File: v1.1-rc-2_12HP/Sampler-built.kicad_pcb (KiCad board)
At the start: 4 copper layers, 60.5 x 109.2 mm, 231 parts, among them J10 Eurorack_Power_10pin_Unshroud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, J11 3.5mm_Mono_Switched, J12 3.5mm_Mono_Switched, J13 3.5mm_Mono_Switched, J14 3.5mm_Mono_Switched, J15 3.5mm_Mono_Switched, J16 3.5mm_Mono_Switched, J17 3.5mm_Mono_Switched, J2 3.5mm_Mono_Switched, J3 Conn_01x04, J4 Conn_02x04, J6 3.5mm_Mono_Switched, J7 3.5mm_Mono_Switched, J8 3.5mm_Mono_Switched, J9 3.5mm_Mono_Switched, U1 TL072H, U10 TL072H, U11 TL072H, U12 TL072H, U13 AP62200WU-7, U14 TL072H, U15 TL072H, U16 TL072H, U2 STM32F746IE, U3 TL072H, U4 SDRAM_IS42S16400J-6BLI-TR, U5 TL072H, U6 NCP51460SN33, U8 TL072H, U9 PCM3060PW, Y1 16MHz_18pF_FA238

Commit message: Created rc-2
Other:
- board text added: "4ms Sampler v1.1-rc2"
- board text removed: "4ms Sampler v1.1-rc1"
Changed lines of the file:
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@@
 		(tags "resistor 0603")
 		(property "Reference" "R79"
-			(at 0.013352 -1.230078 360)
+			(at 0.013352 -1.230078 0)
 			(layer "F.SilkS")
 			(effects
@@
 		)
 		(property "Value" "33k_0603"
-			(at 0 1.45 360)
+			(at 0 1.45 0)
 			(layer "F.Fab")
 			(effects
@@
 		)
 		(property "Display" "33k"
-			(at 0 0 360)
+			(at 0 0 0)
 			(layer "F.Fab")
 			(hide yes)
@@
 		)
 		(property "JLCPCB ID" "C126359"
-			(at 0 0 360)
+			(at 0 0 0)
 			(layer "F.Fab")
 			(hide yes)
@@
 		)
 		(property "Manufacturer" "Yageo"
-			(at 0 0 360)
+			(at 0 0 0)
 			(layer "F.Fab")
 			(hide yes)
@@
 		)
 		(property "Part Number" "RC0603FR-0733KL"
-			(at 0 0 360)
+			(at 0 0 0)
 			(layer "F.Fab")
 			(hide yes)
@@
 		)
 		(property "Production Stage" "A"
-			(at 0 0 360)
+			(at 0 0 0)
 			(layer "F.Fab")
 			(hide yes)
@@
 		)
 		(property "Specifications" "33k, 1%, 1/10W, 0603"
-			(at 0 0 360)
+			(at 0 0 0)
 			(layer "F.Fab")
 			(hide yes)
@@
 		(tags "resistor 0603")
 		(property "Reference" "R80"
-			(at -2.59 -0.59 360)
+			(at -2.59 -0.59 0)
 			(layer "F.SilkS")
 			(effects
@@
 		)
 		(property "Value" "33k_0603"
-			(at 0 1.45 360)
+			(at 0 1.45 0)
 			(layer "F.Fab")
 			(effects
@@
 		)
 		(property "Display" "33k"
-			(at 0 0 360)
+			(at 0 0 0)
 			(layer "F.Fab")
 			(hide yes)
@@
 		)
 		(property "JLCPCB ID" "C126359"
-			(at 0 0 360)
+			(at 0 0 0)
 			(layer "F.Fab")
 			(hide yes)
@@
 		)
 		(property "Manufacturer" "Yageo"
-			(at 0 0 360)
+			(at 0 0 0)
 			(layer "F.Fab")
 			(hide yes)
@@
 		)
 		(property "Part Number" "RC0603FR-0733KL"
-			(at 0 0 360)
+			(at 0 0 0)
 			(layer "F.Fab")
 			(hide yes)
@@
 		)
 		(property "Production Stage" "A"
-			(at 0 0 360)
+			(at 0 0 0)
 			(layer "F.Fab")
 			(hide yes)
@@
 		)
 		(property "Specifications" "33k, 1%, 1/10W, 0603"
-			(at 0 0 360)
+			(at 0 0 0)
 			(layer "F.Fab")
 			(hide yes)
@@
 		(tags "resistor 0603")
 		(property "Reference" "R77"
-			(at 0.05 -1.25 360)
+			(at 0.05 -1.25 0)
 			(layer "F.SilkS")
 			(effects
@@
 		)
 		(property "Value" "33k_0603"
-			(at 0 1.45 360)
+			(at 0 1.45 0)
 			(layer "F.Fab")
 			(effects
@@
 		)
 		(property "Display" "33k"
-			(at 0 0 360)
+			(at 0 0 0)
 			(layer "F.Fab")
 			(hide yes)
@@
 		)
 		(property "JLCPCB ID" "C126359"
-			(at 0 0 360)
+			(at 0 0 0)
 			(layer "F.Fab")
 			(hide yes)
@@
 		)
 		(property "Manufacturer" "Yageo"
-			(at 0 0 360)
+			(at 0 0 0)
 			(layer "F.Fab")
 			(hide yes)
@@
 		)
 		(property "Part Number" "RC0603FR-0733KL"
-			(at 0 0 360)
+			(at 0 0 0)
 			(layer "F.Fab")
 			(hide yes)
@@
 		)
 		(property "Production Stage" "A"
-			(at 0 0 360)
+			(at 0 0 0)
 			(layer "F.Fab")
 			(hide yes)
@@
 		)
 		(property "Specifications" "33k, 1%, 1/10W, 0603"
-			(at 0 0 360)
+			(at 0 0 0)
 			(layer "F.Fab")
 			(hide yes)
@@
 		(descr "C1206")
 		(property "Reference" "C43"
-			(at -4.2266 0.119079 360)
+			(at -4.2266 0.119079 0)
 			(layer "F.SilkS")
 			(effects
@@
 		)
 		(property "Value" "4.7uF_1206_lowESR"
-			(at 1.05 -1.4 360)
+			(at 1.05 -1.4 0)
 			(layer "F.Fab")
 			(effects
@@
 		)
 		(property "Display" "4.7uF/16V/100mΩ"
-			(at 0 0 360)
+			(at 0 0 0)
 			(layer "F.Fab")
 			(hide yes)
@@
 		)
 		(property "Manufacturer" "Taiyo Yuden"
-			(at 0 0 360)
+			(at 0 0 0)
 			(layer "F.Fab")
 			(hide yes)
@@
 		)
 		(property "Part Number" "EMF316AB7475KLHT"
-			(at 0 0 360)
+			(at 0 0 0)
 			(layer "F.Fab")
 			(hide yes)
@@
 		)
 		(property "Production Stage" "A"
-			(at 0 0 360)
+			(at 0 0 0)
 			(layer "F.Fab")
 			(hide yes)
@@
 		)
 		(property "Specifications" "4.7uF, Min. 16V, ESR<=100mΩ@1MHz, 1206, MLCC"
-			(at 0 0 360)
+			(at 0 0 0)
 			(layer "F.Fab")
 			(hide yes)
@@
 		(tags "resistor 0603")
 		(property "Reference" "R78"
-			(at 0.013352 -1.260078 360)
+			(at 0.013352 -1.260078 0)
 			(layer "F.SilkS")
 			(effects
@@
 		)
 		(property "Value" "33k_0603"
-			(at 0 1.45 360)
+			(at 0 1.45 0)
 			(layer "F.Fab")
 			(effects
@@
 		)
 		(property "Display" "33k"
-			(at 0 0 360)
+			(at 0 0 0)
 			(layer "F.Fab")
 			(hide yes)
@@
 		)
 		(property "JLCPCB ID" "C126359"
-			(at 0 0 360)
+			(at 0 0 0)
 			(layer "F.Fab")
 			(hide yes)
@@
 		)
 		(property "Manufacturer" "Yageo"
-			(at 0 0 360)
+			(at 0 0 0)
 			(layer "F.Fab")
 			(hide yes)
@@
 		)
 		(property "Part Number" "RC0603FR-0733KL"
-			(at 0 0 360)
+			(at 0 0 0)
 			(layer "F.Fab")
 			(hide yes)
@@
 		)
 		(property "Production Stage" "A"
-			(at 0 0 360)
+			(at 0 0 0)
 			(layer "F.Fab")
 			(hide yes)
@@
 		)
 		(property "Specifications" "33k, 1%, 1/10W, 0603"
-			(at 0 0 360)
+			(at 0 0 0)
 			(layer "F.Fab")
 			(hide yes)
@@
 		(tags "MicroSD SDCard")
 		(property "Reference" "SD1"
-			(at 7.709922 -3.023352 360)
+			(at 7.709922 -3.023352 0)
 			(layer "B.SilkS")
 			(effects
@@
 		)
 		(property "Value" "microSDCon_Vert_TH_PJS008U-3000"
-			(at 0.65 -3.72 270)
+			(at 0.65 -3.72 -90)
 			(layer "B.Fab")
 			(effects
@@
 		)
 		(property "Manufacturer" "Yamaichi"
-			(at 0 0 360)
+			(at 0 0 0)
 			(layer "B.Fab")
 			(hide yes)
@@
 		)
 		(property "Part Number" "PJS008U-3000-0"
-			(at 0 0 360)
+			(at 0 0 0)
 			(layer "B.Fab")
 			(hide yes)
@@
 		)
 		(property "Production Stage" "AB"
-			(at 0 0 360)
+			(at 0 0 0)
 			(layer "B.Fab")
 			(hide yes)
@@
 		)
 		(property "Specifications" "MicroSD Card Conn Ver Dip Mnt"
-			(at 0 0 360)
+			(at 0 0 0)
 			(layer "B.Fab")
 			(hide yes)
@@
 		(layer "Edge.Cuts")
 	)
-	(gr_text "4ms Sampler\nv1.1-rc1"
+	(gr_text "4ms Sampler\nv1.1-rc2"
 		(at 185.45 35.43 0)
 		(layer "F.SilkS")
@@
 			)
 		)
-		(render_cache "4ms Sampler\nv1.1-rc1" 0
+		(render_cache "4ms Sampler\nv1.1-rc2" 0
 			(polygon
 				(pts
@@
 			(polygon
 				(pts
-					(xy 189.115401 35.697981) (xy 188.858067 36.936) (xy 188.506651 36.936) (xy 188.670196 36.149049)
-					(xy 188.617503 36.182961) (xy 188.562594 36.214171) (xy 188.510754 36.2402) (xy 188.453029 36.265228)
-					(xy 188.392266 36.287948) (xy 188.331248 36.3083) (xy 188.289763 36.321094) (xy 188.352778 36.018916)
-					(xy 188.418593 35.997443) (xy 188.479091 35.974568) (xy 188.534272 35.950292) (xy 188.59193 35.920198)
-					(xy 188.642352 35.888198) (xy 188.694137 35.847953) (xy 188.742223 35.802835) (xy 188.786608 35.752844)
-					(xy 188.822409 35.705106) (xy 188.827293 35.697981)
+					(xy 189.075248 36.936) (xy 188.069358 36.936) (xy 188.091216 36.875202) (xy 188.117443 36.816569)
+					(xy 188.148039 36.7601) (xy 188.183004 36.705795) (xy 188.222338 36.653653) (xy 188.23642 36.636753)
+					(xy 188.276209 36.593682) (xy 188.32377 36.548551) (xy 188.379101 36.501359) (xy 188.42896 36.462121)
+					(xy 188.483794 36.421565) (xy 188.5436 36.379689) (xy 188.60838 36.336495) (xy 188.625353 36.32549)
+					(xy 188.683412 36.287128) (xy 188.733393 36.252497) (xy 188.781495 36.216807) (xy 188.827183 36.178381)
+					(xy 188.841654 36.163997) (xy 188.878223 36.117642) (xy 188.902324 36.062001) (xy 188.899006 36.002784)
+					(xy 188.883566 35.977004) (xy 188.830924 35.945268) (xy 188.79857 35.941833) (xy 188.739076 35.953)
+					(xy 188.692764 35.981401) (xy 188.654039 36.029318) (xy 188.626131 36.085621) (xy 188.609526 36.129998)
+					(xy 188.266902 36.100396) (xy 188.287472 36.04506) (xy 188.312903 35.987039) (xy 188.343856 35.92935)
+					(xy 188.376825 35.880858) (xy 188.389707 35.865043) (xy 188.431562 35.822532) (xy 188.478981 35.786002)
+					(xy 188.531964 35.755453) (xy 188.563803 35.741066) (xy 188.620077 35.722216) (xy 188.684264 35.708752)
+					(xy 188.746919 35.701389) (xy 188.815633 35.69815) (xy 188.836378 35.697981) (xy 188.899137 35.699424)
+					(xy 188.964853 35.704753) (xy 189.030066 35.715653) (xy 189.090818 35.734045) (xy 189.102505 35.739014)
+					(xy 189.154254 35.768798) (xy 189.199542 35.811545) (xy 189.232638 35.86475) (xy 189.252435 35.925575)
+					(xy 189.257931 35.985018) (xy 189.251519 36.04841) (xy 189.250223 36.054967) (xy 189.232426 36.116309)
+					(xy 189.204752 36.176028) (xy 189.171862 36.22775) (xy 189.142073 36.265699) (xy 189.09974 36.310437)
+					(xy 189.055261 36.35019) (xy 189.003219 36.391241) (xy 188.954073 36.426442) (xy 188.899675 36.462544)
+					(xy 188.864515 36.484639) (xy 188.812455 36.516476) (xy 188.760465 36.548956) (xy 188.712108 36.580773)
+					(xy 188.663217 36.616801) (xy 188.639421 36.635874) (xy 189.137676 36.635874)
 				)
 			)

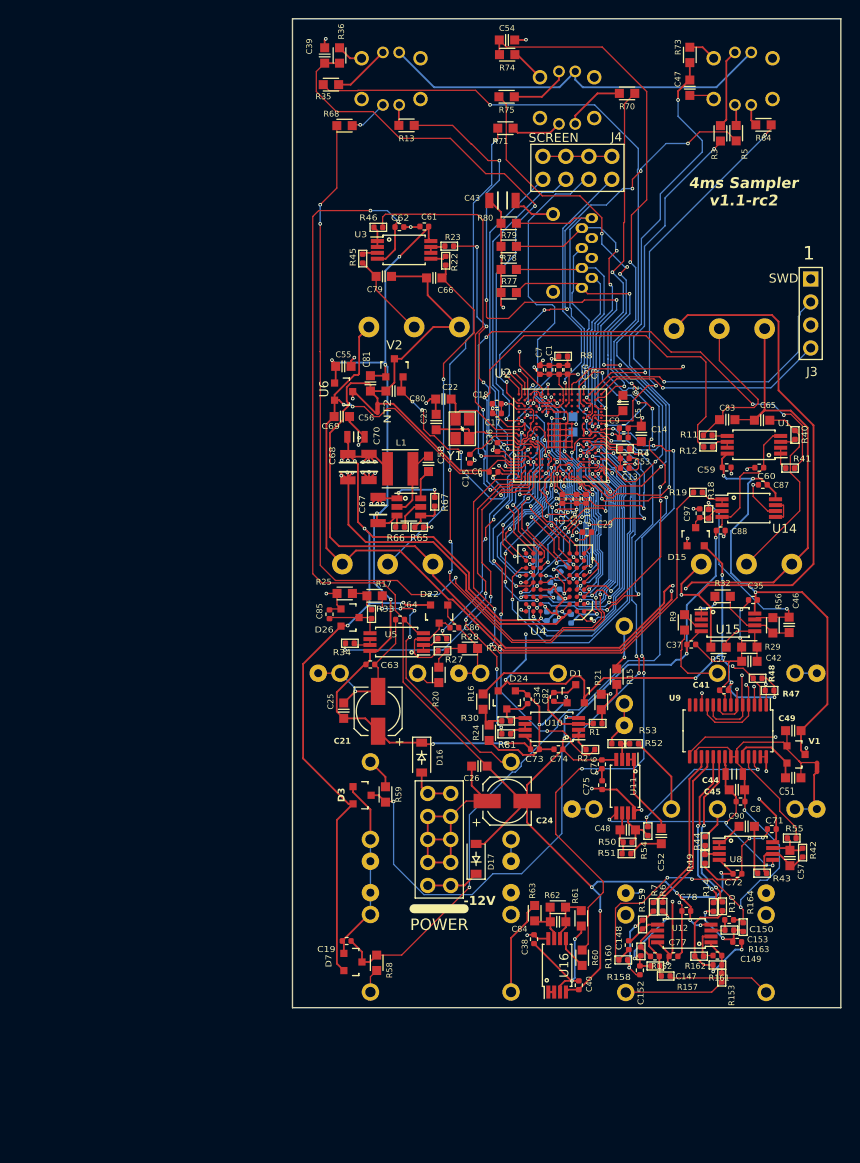
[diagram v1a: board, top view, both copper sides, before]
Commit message: Added softstart to +/-12v rails - and solder jumpers between +12v and regulators/references
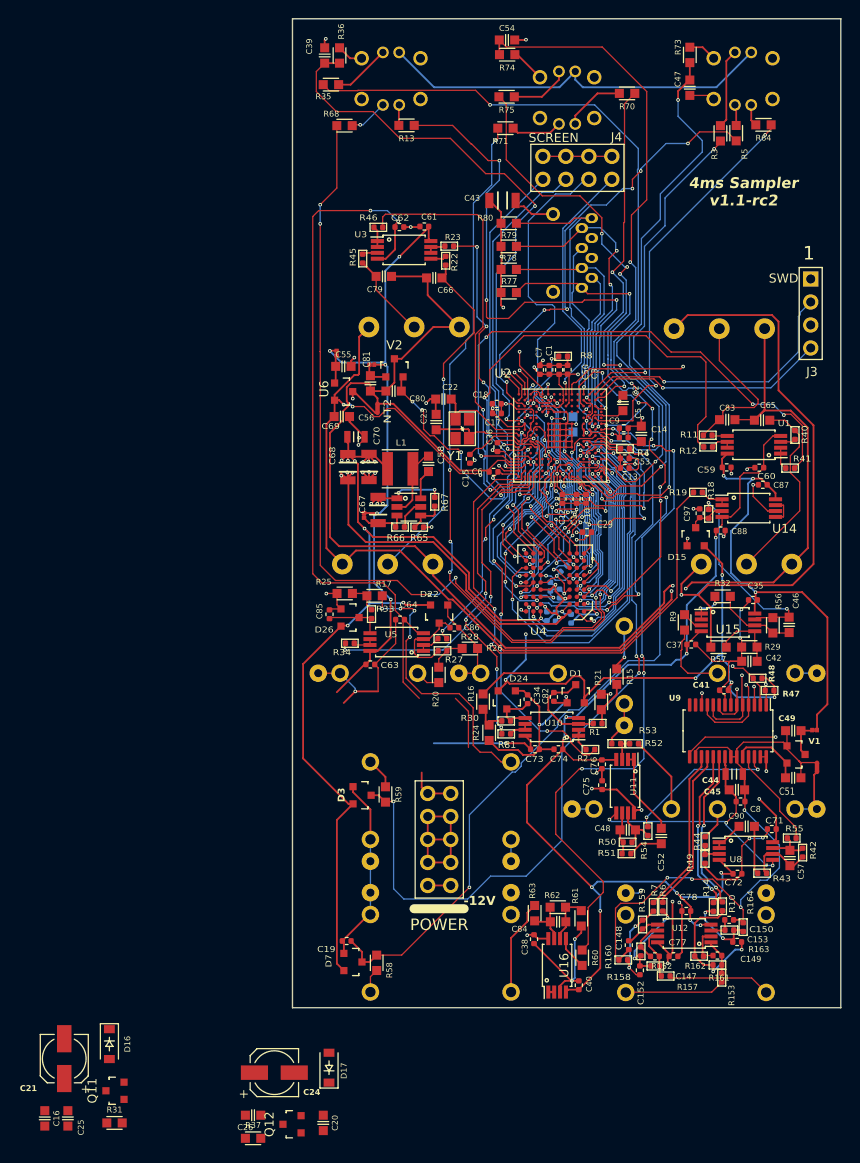
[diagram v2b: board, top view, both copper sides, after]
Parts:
- added C16: 100nF_0603_16V, 4ms_Capacitor:C_0603, F.Cu at (108.3, 137.8)
- added C20: 100nF_0603_16V, 4ms_Capacitor:C_0603, F.Cu at (139.1, 138.2)
- added JP11: JumpForCrystal, 4ms_SolderJumper:JUMPER_SMD_1x2_tiny_shorted, F.Cu at (140.5, 53.2)
- added JP2: JumpForCrystal, 4ms_SolderJumper:JUMPER_SMD_1x2_tiny_shorted, F.Cu at (143.6, 71.2)
- added JP3: JumpForCrystal, 4ms_SolderJumper:JUMPER_SMD_1x2_tiny_shorted, F.Cu at (144.4, 54.5)
- added JP4: JumpForCrystal, 4ms_SolderJumper:JUMPER_SMD_1x2_tiny_shorted, F.Cu at (193.3, 94.9)
- added Q11: Si2347, 4ms_Package_SOT:SOT23-3_PO132, F.Cu at (116.0, 134.7)
- added Q12: Si2318, 4ms_Package_SOT:SOT23-3_PO132, F.Cu at (135.6, 138.4)
- added R31: 1M_0603, 4ms_Resistor:R_0603, F.Cu at (116.0, 138.2)
- added R37: 1M_0603, 4ms_Resistor:R_0603, F.Cu at (131.3, 139.9)
- moved C25 54.4 mm to (110.8, 137.8), turned to -90 degrees
- moved C21 51.7 mm to (110.4, 131.2)
- moved D16 46.8 mm to (115.4, 129.6)
- moved C26 45.9 mm to (131.3, 137.4)
- moved C24 39.5 mm to (133.7, 132.7)
- moved D17 28.2 mm to (139.7, 132.2)
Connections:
- C25 pad 1: +12V -> Net-(D16-K)
- C26 pad 1: -12VA -> Net-(D17-A)
- C49 pad 1: +12V -> Net-(JP4-B)
- C55 pad 1: +12V -> Net-(JP11-B)
- C67 pad 1: +12V -> Net-(JP2-B)
- C81 pad 1: +12V -> Net-(JP3-B)
- D16 pad 1: +12V -> Net-(D16-K)
- D17 pad 2: -12VA -> Net-(D17-A)
- R66 pad 1: +12V -> Net-(JP2-B)
- U13 pad 3: +12V -> Net-(JP2-B)
- U6 pad 1: +12V -> Net-(JP11-B)
- V1 pad 3: +12V -> Net-(JP4-B)
- V2 pad 1: +12V -> Net-(JP3-B)
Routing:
- net +12V: track 241.3 -> 217.1 mm, vias 17 -> 15
- net -12VA: track 225.9 -> 202.3 mm
- net GND: track 364.8 -> 355.5 mm
- net Net-(D17-A): track 0.00 -> 6.02 mm
- net Net-(JP2-B): track 0.00 -> 5.03 mm
- net Net-(JP4-B): track 0.00 -> 4.24 mm
- net Net-(D17-K): track 5.87 -> 2.54 mm
- net Net-(JP3-B): track 0.00 -> 3.02 mm
- net Net-(JP11-B): track 0.00 -> 2.95 mm
- net Net-(J9-SIG): track 28.4 -> 30.8 mm
- net /D13: track 83.8 -> 86.2 mm

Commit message: added power circuit back in, ran DRC. TODO: fix silkscreen
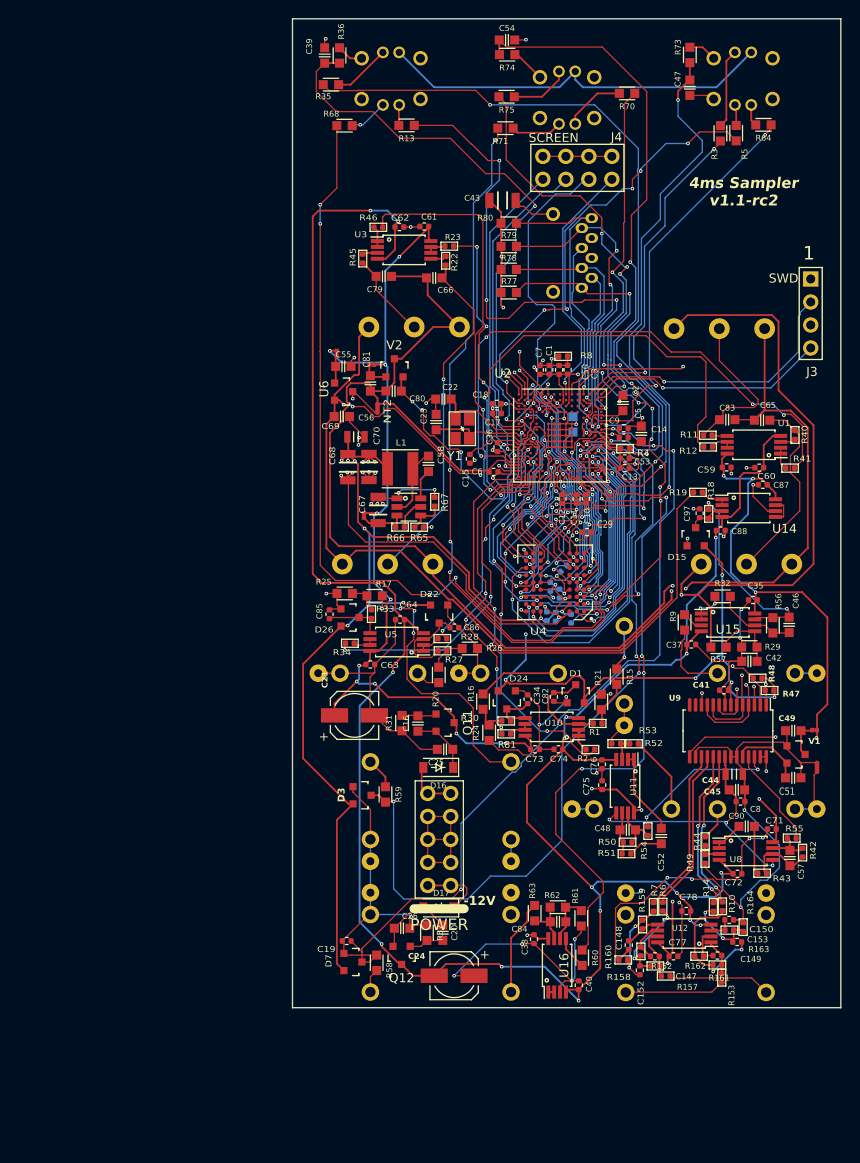
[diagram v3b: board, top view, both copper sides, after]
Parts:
- moved C16 60.0 mm to (149.5, 94.2), turned to 90 degrees
- moved C25 58.3 mm to (152.5, 97.0), turned to 180 degrees
- moved Q11 54.6 mm to (152.5, 94.0), turned to -90 degrees
- moved R31 54.4 mm to (147.8, 94.1), turned to 90 degrees
- moved C21 49.6 mm to (142.5, 93.2), turned to 0 degrees
- moved D16 47.5 mm to (151.8, 99.0), turned to 180 degrees
- moved R37 29.7 mm to (150.5, 117.2), turned to -90 degrees
- moved C26 26.4 mm to (147.8, 116.8), turned to 0 degrees
- moved C20 24.8 mm to (152.2, 117.2)
- moved C24 22.6 mm to (153.5, 122.0), turned to 180 degrees
- moved Q12 22.2 mm to (147.7, 119.8), turned to 180 degrees
- moved D17 21.4 mm to (151.8, 114.5), turned to 180 degrees
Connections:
- C19 pad 1: /D2 -> GND
- D7 pad 3: /D2 -> GND
- R58 pad 2: /D2 -> GND
- U2 pad G15: /D2 -> GND
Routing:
- net GND: track 355.5 -> 473.3 mm, vias 57 -> 63
- net /D2: track 87.2 -> 0.00 mm, vias 4 -> 0
- net -12VA: track 202.3 -> 258.6 mm, vias 12 -> 16
- net +12V: track 217.1 -> 234.5 mm, vias 15 -> 20
- net Net-(D16-K): track 0.00 -> 6.57 mm
- net Net-(D17-K): track 2.54 -> 7.22 mm
- net Net-(Q12-G): track 0.00 -> 3.87 mm
- net Net-(Q11-G): track 0.00 -> 3.50 mm
- net Net-(D17-A): track 6.02 -> 8.67 mm
- net GNDA: track 66.3 -> 65.7 mm

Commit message: production files exported
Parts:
- moved D17 4.13 mm to (150.3, 118.4)
- moved C20 3.93 mm to (152.0, 121.2)
- moved R37 3.93 mm to (150.2, 121.2)
- moved C26 3.59 mm to (147.6, 120.3)
- moved Q12 3.48 mm to (147.6, 123.2)
- moved C24 2.35 mm to (155.7, 121.2), turned to -90 degrees
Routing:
- net -12VA: track 258.6 -> 268.8 mm
- net Net-(D17-K): track 7.22 -> 11.3 mm
- net GND: track 473.3 -> 471.8 mm, vias 63 -> 65
- net +3V3: track 401.2 -> 401.9 mm
